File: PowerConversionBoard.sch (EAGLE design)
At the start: 32 parts, among them Q1 MOSFET_PCH-NDS8434, U3 AZ1117EH-3.3TRG1

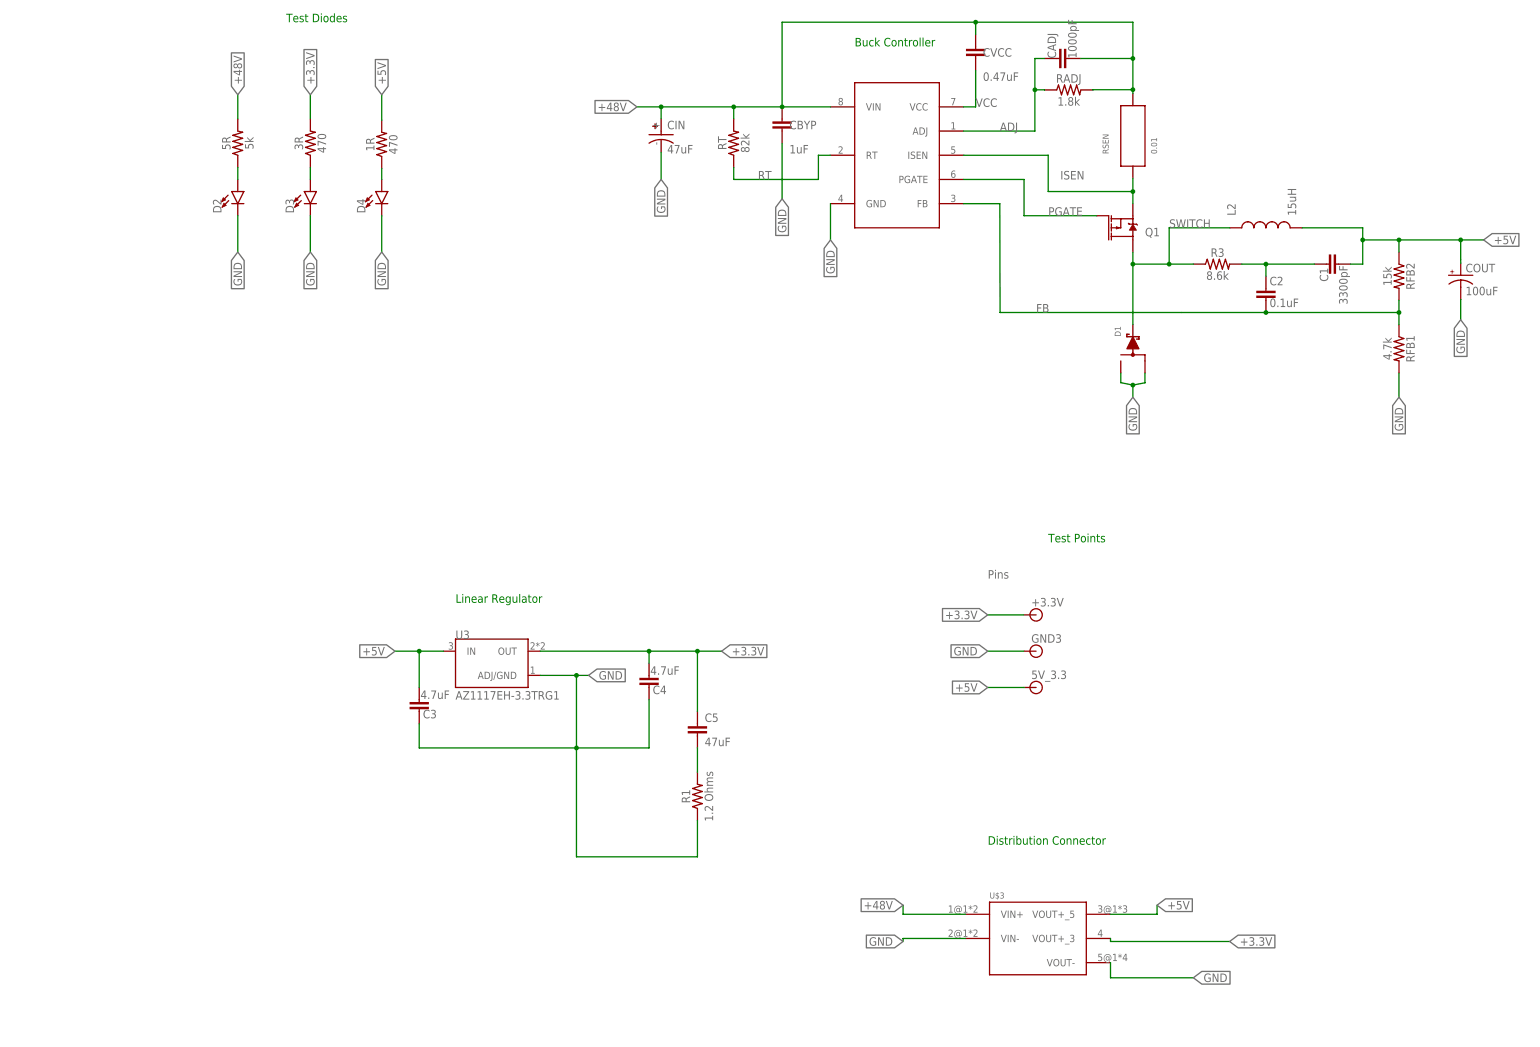
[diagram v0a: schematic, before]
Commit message: Cleaning up git and adding exports for ordering
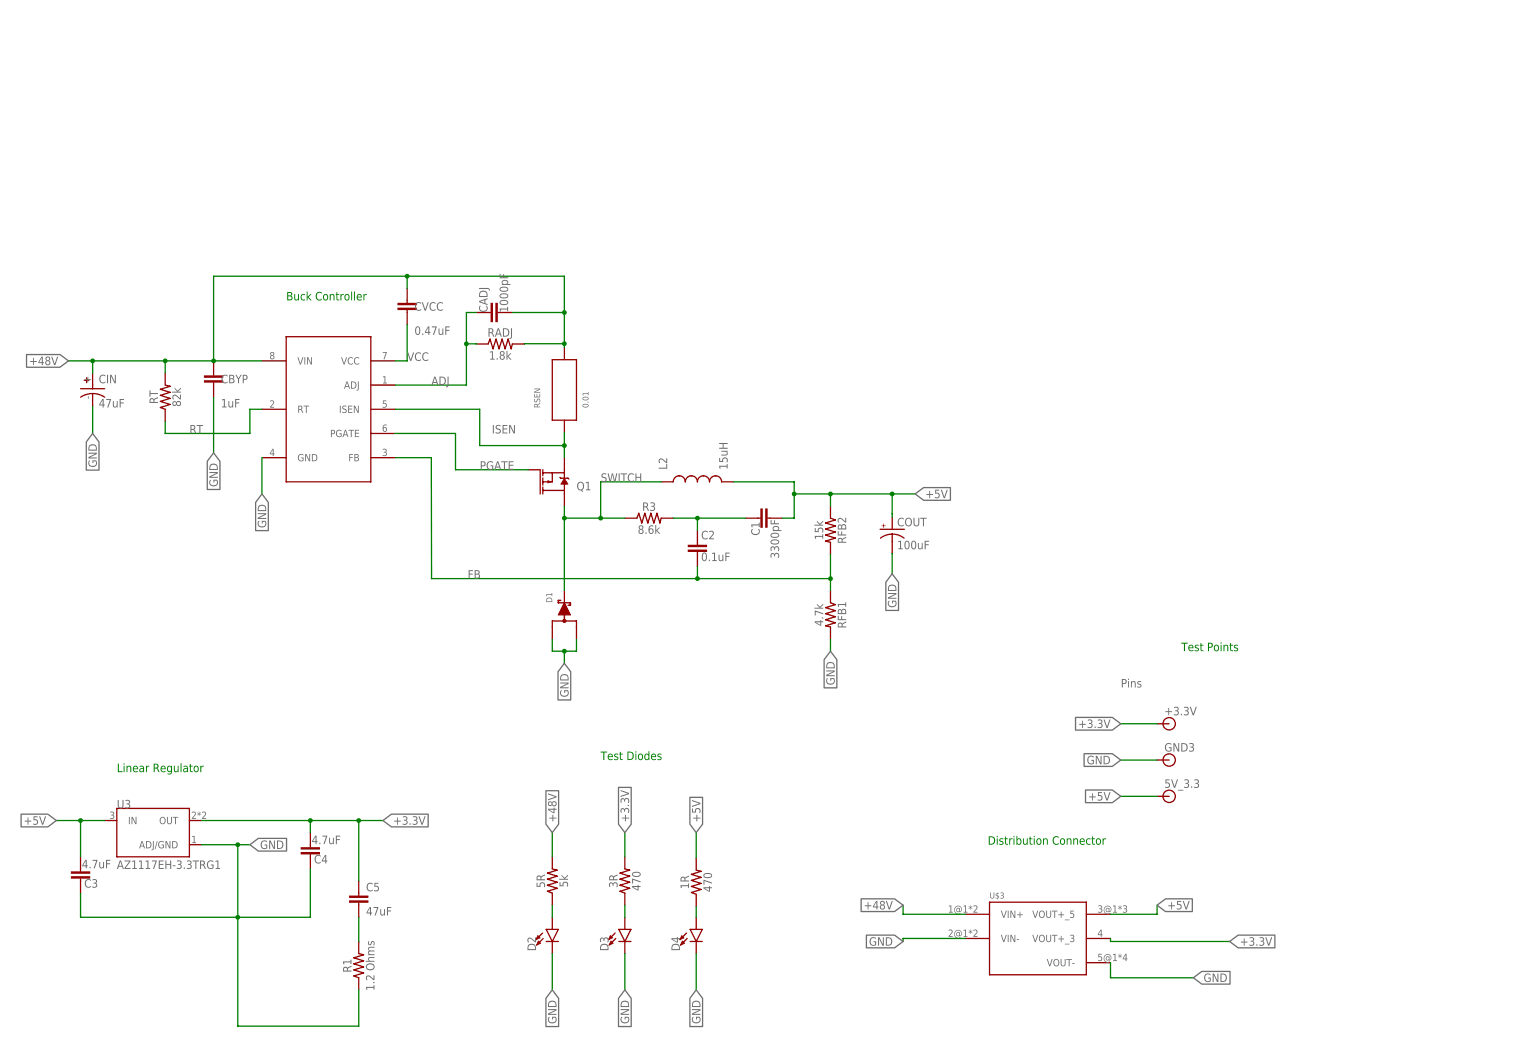
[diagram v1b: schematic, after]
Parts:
- D1: device PowerComponents:SWITCHMODE_SCHOTTKY -> Schottky Diode 8A - MBRD835LT4G:SWITCHMODE_SCHOTTKY
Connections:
- new net N$1: U$1.FB
- net FB: no longer U$1.FB
- net GND: now also D1.A@1, D1.A@2; no longer D1.P$1, D1.P$3
- net SWITCH: now also D1.C; no longer D1.P$4
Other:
- moved on the sheet: +3.3V, 1R, 3R, 5R, 5V_3.3, C1, C2, C3, C4, C5, CADJ, CBYP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

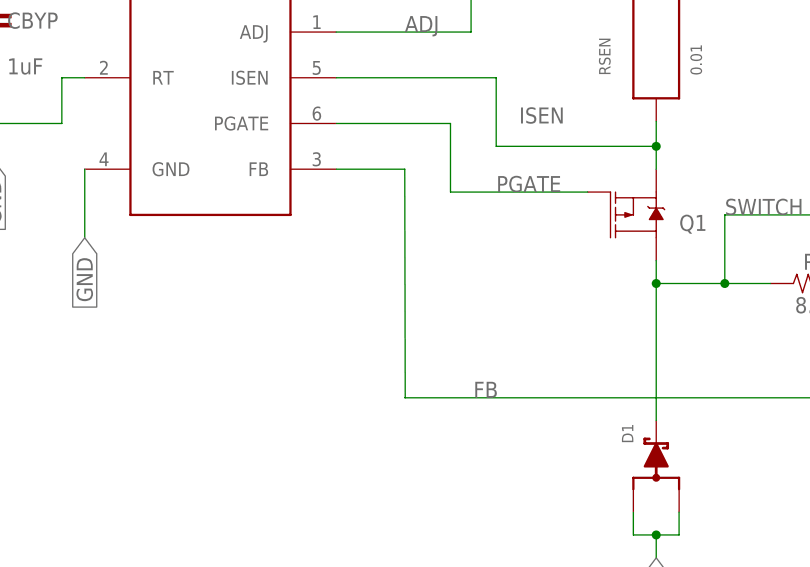
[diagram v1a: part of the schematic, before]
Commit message: playing with 3d models generated by eagle package
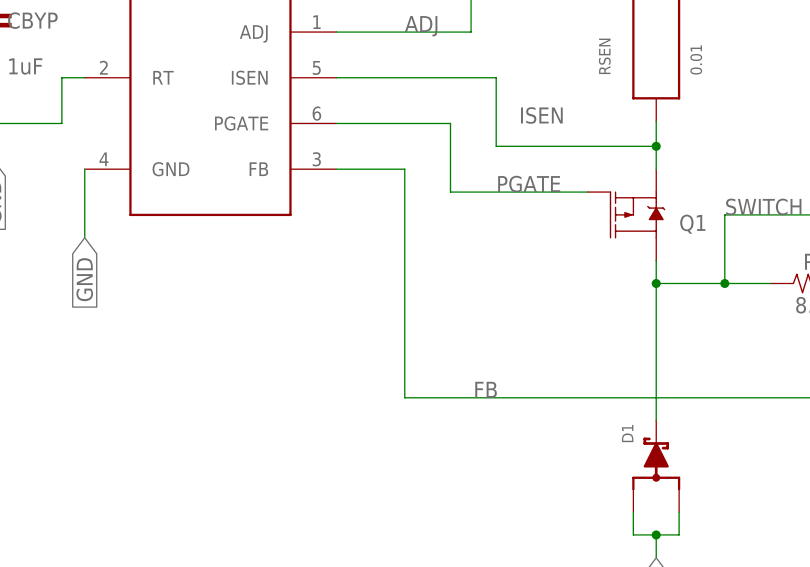
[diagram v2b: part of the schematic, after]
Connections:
- removed net N$1: U$1.FB
- net FB: now also U$1.FB
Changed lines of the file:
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@@
 <part name="R1" library="SparkFun-Resistors" library_urn="urn:adsk.eagle:library:532" deviceset="1.6KOHM" device="-0603-1/10W-1%" package3d_urn="urn:adsk.eagle:package:39650/1" value="1.2 Ohms"/>
 <part name="COUT" library="PowerComponents" deviceset="C-TANTALUM(10UF_150UF)" device="" value="100uF"/>
-<part name="D1" library="Schottky Diode 8A - MBRD835LT4G" deviceset="SWITCHMODE_SCHOTTKY" device=""/>
+<part name="D1" library="Schottky Diode 8A - MBRD835LT4G" deviceset="SWITCHMODE_SCHOTTKY" device="" package3d_urn="urn:adsk.eagle:package:25915513/1"/>
 <part name="RSEN" library="INA4181A4" deviceset="CSS2H-2512" device="" value="0.01"/>
 <part name="U$3" library="Dist_Convert_Connector" deviceset="CON2DIST" device=""/>
@@
 <wire x1="152.4" y1="106.68" x2="96.52" y2="106.68" width="0.1524" layer="91"/>
 <junction x="152.4" y="106.68"/>
+<pinref part="U$1" gate="G$1" pin="FB"/>
+<wire x1="96.52" y1="132.08" x2="88.9" y2="132.08" width="0.1524" layer="91"/>
+<wire x1="96.52" y1="106.68" x2="96.52" y2="132.08" width="0.1524" layer="91"/>
 </segment>
 </net>
@@
 </segment>
 </net>
-<net name="N$1" class="0">
-<segment>
-<pinref part="U$1" gate="G$1" pin="FB"/>
-<wire x1="96.52" y1="132.08" x2="88.9" y2="132.08" width="0.1524" layer="91"/>
-<wire x1="96.5708" y1="106.68" x2="96.52" y2="132.08" width="0.1524" layer="91"/>
-</segment>
-</net>

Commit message: Reeeeeeeeeev 2 on the red line
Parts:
- removed +3.3V, 5V_3.3, GND3: (no value), SparkFun-Connectors:BANANA_CONN
- removed RSEN: 0.01, INA4181A4:CSS2H-2512
- added C6: 3300pF, SparkFun-Capacitors:12PF-0603-50V-5%
- added C7: 0.1uF, SparkFun-Capacitors:12PF-0603-50V-5%
- added C8, C9: 1.0uF, SparkFun-Capacitors:1.0UF-0603-16V-10%
- added CADJ1: 1000pF, SparkFun-Capacitors:5.6PF-0603-50V-5%
- added CBYP1: 1uF, SparkFun-Capacitors:3.3NF-0603-100V-10%
- added CIN1: 47uF, brick-capacitor-UCM1H331MNL1GS:UCM1H331MNL1GS
- added COUT1: 100uF, PowerComponents:C-TANTALUM(10UF_150UF)
- added CVCC1: 0.47uF, SparkFun-Capacitors:5.6PF-0603-50V-5%
- added D5: SWITCHMODE_SCHOTTKY, Schottky Diode 8A - MBRD835LT4G:SWITCHMODE_SCHOTTKY
- added J1, J2, J3, J4, J5: (no value), SparkFun-Connectors:CONN_01
- added J6, J7, J8, J9: (no value), Banana Plug PTH:BANANA_PTH
- added JP1, JP2: JUMPER-SMT_2_NO_SILK, SparkFun-Jumpers:JUMPER-SMT_2_NO_SILK
- added L1: 15uH, Inductor_15uH - hcma1305:HCMA1305
- added Q2: MOSFET_PCH-NDS8434, SparkFun-DiscreteSemi:MOSFET_PCH-NDS8434
- added R2: 8.6k, SparkFun-Resistors:RESISTOR0603
- added R4: (no value), SparkFun-Resistors:RESISTOR0603
- added RADJ1: 1.8k, SparkFun-Resistors:RESISTOR0603
- added RFB3: 4.7k, SparkFun-Resistors:RESISTOR0603
- added RFB4: 15k, SparkFun-Resistors:RESISTOR0603
- added RT1: 82k, SparkFun-Resistors:82OHM-0603-1/10W-1%
- added U$2: LM5085, Buck_Controller:LM5085
- added U$4: ADP7159ARDZ-04-R7, Linear Regulator - ADP7159:ADP7159ARDZ-04-R7
- C5: value 47uF -> 1.0uF; device SparkFun-Capacitors:0.1UF-0603-25V-5% -> SparkFun-Capacitors:1.0UF-0603-16V-10%
- R1: value 1.2 Ohms -> (none); device SparkFun-Resistors:1.6KOHM-0603-1/10W-1% -> SparkFun-Resistors:RESISTOR0603
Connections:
- net ADJ renamed ADJ2
- net FB renamed FB2
- net PGATE renamed PGATE2
- net RT renamed RT2
- net VCC renamed VCC2
- removed net +3.3V: +3.3V.1, 3R.2, C4.1, C5.1, U$3.VOUT+_3, U3.OUT
- removed net +48V: 5R.2, CADJ.2, CBYP.1, CIN.+, CVCC.1, RADJ.2, RSEN.2, RT.2, U$1.VIN, U$3.VIN+
- removed net +5V: 1R.2, 5V_3.3.1, C1.1, C3.1, COUT.+, L2.2, RFB2.1, U$3.VOUT+_5, U3.IN
- removed net ISEN: Q1.S, RSEN.1, U$1.ISEN
- removed net N$12: C5.2, R1.2
- removed net SWITCH: D1.C, L2.1, Q1.D, R3.1
- new net 18V: C6.1, CADJ.2, CBYP.1, CIN.+, CVCC.1, J2.1, L1.2, Q1.S, RADJ.2, RFB4.1, RT.2, U$1.VIN
- new net 3V3: 3R.2, C4.1, J4.1, J6.1, U$3.VOUT+_3, U$4.VOUT, U$4.VOUT_SENSE, U3.OUT
- new net 48V: 5R.2, CADJ1.2, CBYP1.1, CIN1.+, CVCC1.1, J1.1, J9.1, Q2.S, RADJ1.2, RT1.2, U$2.VIN, U$3.VIN+
- new net 5V: 1R.2, C1.1, C3.1, COUT.+, COUT1.+, J3.1, J8.1, L2.2, RFB2.1, U$3.VOUT+_5, U$4.EN, U$4.VIN, U3.IN
- new net ADJ1: CADJ1.1, RADJ1.1, U$2.ADJ
- new net BYP: C5.1, U$4.BYP
- new net FB1: C7.2, RFB3.1, RFB4.2, U$2.FB
- new net ISEN1: JP1.2, U$2.ISEN
- new net ISEN2: JP2.1, U$1.ISEN
- new net N$1: C6.2, C7.1, R2.2
- new net PGATE1: Q2.G, U$2.PGATE
- new net REF: C9.1, R1.2, U$4.REF
- new net REF_SENSE: R1.1, R4.2, U$4.REF_SENSE
- new net RT1: RT1.1, U$2.RT
- new net SWITCH1: D5.C, JP1.1, L1.1, Q2.D, R2.1
- new net SWITCH2: D1.C, JP2.2, L2.1, Q1.D, R3.1
- new net VCC1: CVCC1.2, U$2.VCC
- new net VREG: C8.1, U$4.VREG
- net GND: now also C5.2, C8.2, C9.2, CBYP1.2, CIN1.-, COUT1.-, D5.A@1, D5.A@2, J5.1, J7.1, R4.1, RFB3.2, U$2.GND, U$4.GND; no longer GND3.1, R1.1

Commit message: Larger LEDs on main and graphic and text on the other
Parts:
- removed COUT1: 100uF, PowerComponents:C-TANTALUM(10UF_150UF)
- added COUT2_2: 150uF, PowerComponents:C-TANTALUM(10UF_150UF)
- CIN1: value 47uF -> 100uF
- COUT1_2: value 100uF -> 150uF
- D2, D3, D4: value (none) -> COLOR; device SparkFun-LED:LED0603 -> LED-0805:LED-0805
- L1: value 15uH -> 18uH
- L2: value 15uH -> 3uH
- R2_1: value 8.6k -> 400k
- R3_2: value 8.6k -> 155k
- RADJ: value 1.8k -> 5k
- RFB1_1: value 4.7k -> 5.6k
- RFB2_1: value 15k -> 75k
- RT1: value 82k -> 366k
- RT_2: value 82k -> 97k
- renumbered C1 to C1_2, C2 to C2_2, C6 to C1_1, C7 to C2_1, CIN to CIN2, COUT to COUT1_2, R2 to R2_1, R3 to R3_2, RFB3 to RFB1_1, RFB4 to RFB2_1, RT to RT_2
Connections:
- net 5V: now also COUT2_2.+; no longer COUT1.+
- net GND: now also COUT2_2.-; no longer COUT1.-
